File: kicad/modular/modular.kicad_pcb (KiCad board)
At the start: 2 copper layers, 50.5 x 78 mm, 53 parts, among them J1 CONN_PWR, J2 HEADER, J3 HEADER, U1 LM317, U2 LM337, U3 REF5010, U4 OPA4197

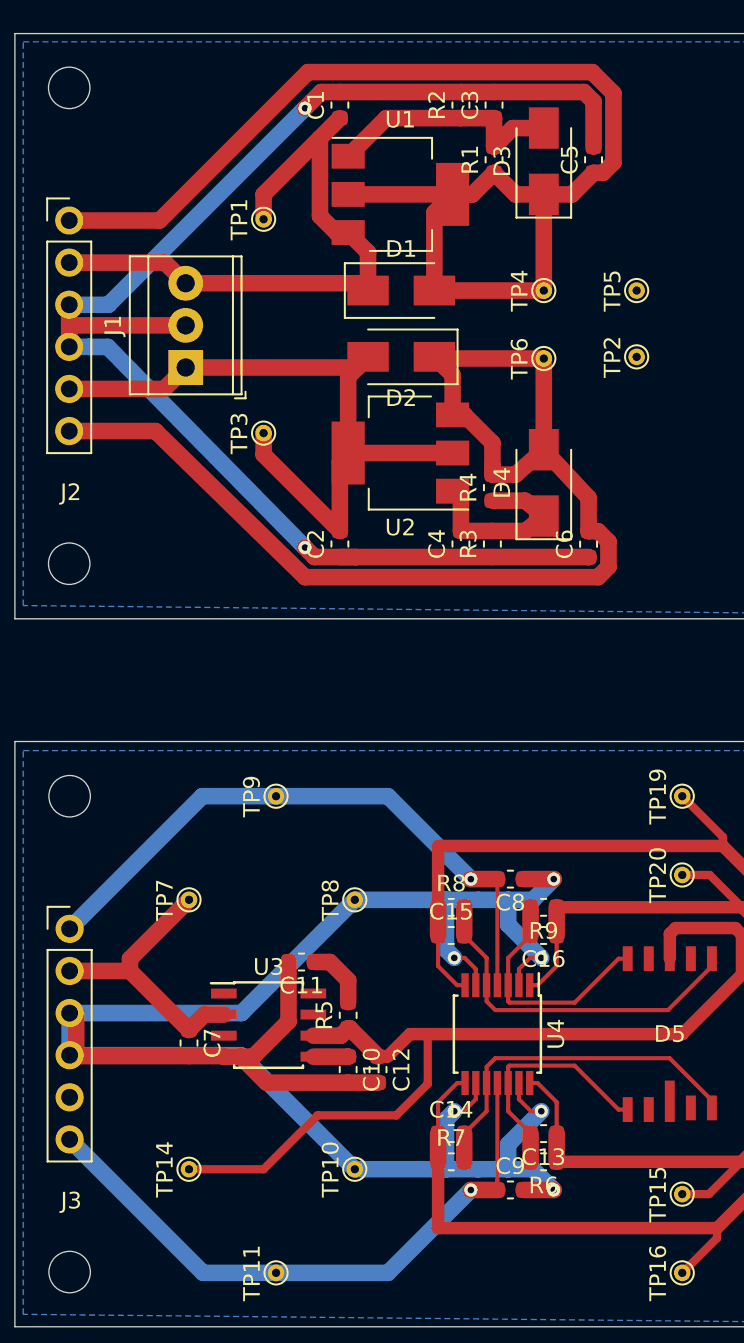
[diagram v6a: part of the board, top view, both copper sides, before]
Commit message: removed overlap of component labels in modular boards
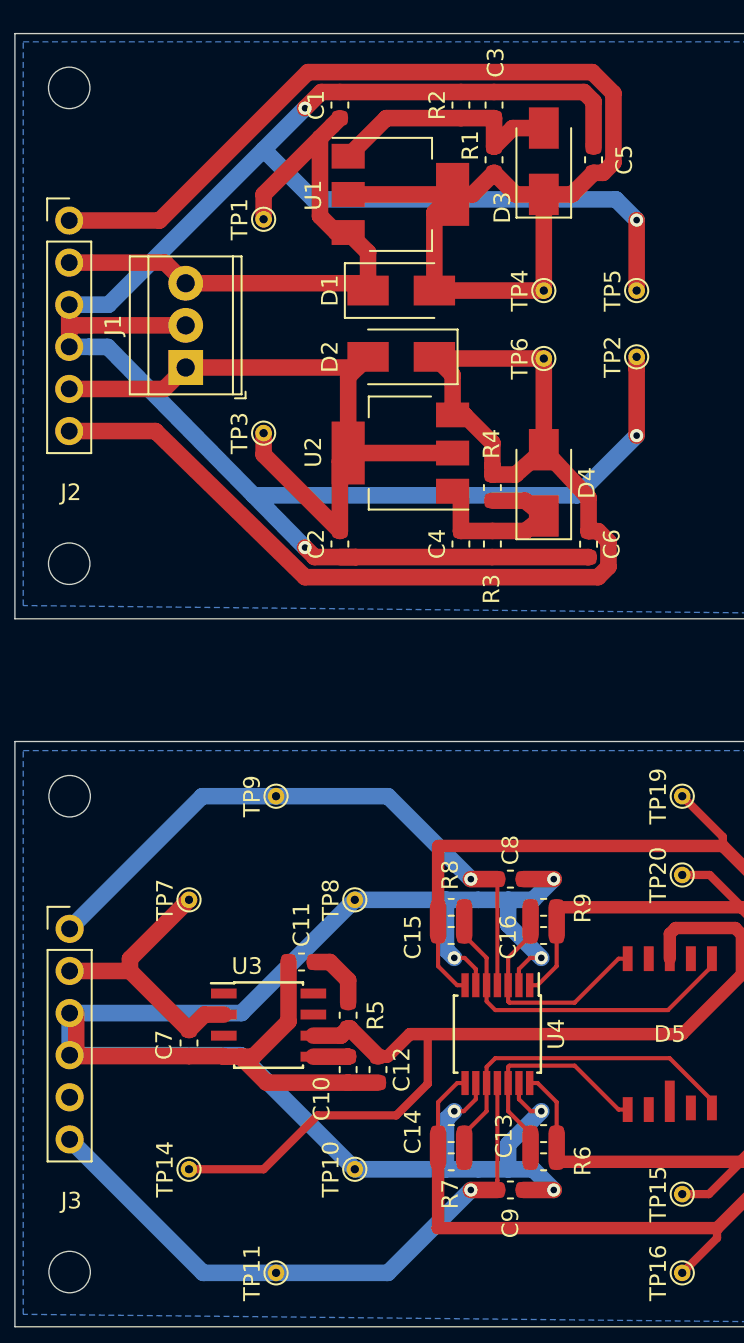
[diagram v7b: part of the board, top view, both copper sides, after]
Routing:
- net GND: track 213.7 -> 271.5 mm, vias 8 -> 10
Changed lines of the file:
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@@
     (thickness 1.6)
     (drawings 8)
-    (tracks 278)
+    (tracks 292)
     (zones 0)
     (modules 53)
@@
     (47 F.CrtYd user)
     (48 B.Fab user)
-    (49 F.Fab user)
+    (49 F.Fab user hide)
   )
   (setup
@@
     (tags "SOIC 1.27")
     (attr smd)
-    (fp_text reference U3 (at 0 -3.5) (layer F.SilkS)
+    (fp_text reference U3 (at -1.3 -3.555) (layer F.SilkS)
       (effects (font (size 1 1) (thickness 0.15)))
     )
@@
     (tags capacitor)
     (attr smd)
-    (fp_text reference C3 (at 0 -1.43 90) (layer F.SilkS)
+    (fp_text reference C3 (at 2.5625 0.1 90) (layer F.SilkS)
       (effects (font (size 1 1) (thickness 0.15)))
     )
@@
     (tags capacitor)
     (attr smd)
-    (fp_text reference C5 (at 0 -1.43 90) (layer F.SilkS)
+    (fp_text reference C5 (at 0 1.85 90) (layer F.SilkS)
       (effects (font (size 1 1) (thickness 0.15)))
     )
@@
     (tags capacitor)
     (attr smd)
-    (fp_text reference C6 (at 0 -1.43 90) (layer F.SilkS)
+    (fp_text reference C6 (at 0 1.4 90) (layer F.SilkS)
       (effects (font (size 1 1) (thickness 0.15)))
     )
@@
     (tags capacitor)
     (attr smd)
-    (fp_text reference C7 (at 0 -1.43 90) (layer F.SilkS)
+    (fp_text reference C7 (at 0.1125 1.5 270) (layer F.SilkS)
       (effects (font (size 1 1) (thickness 0.15)))
     )
@@
     (tags capacitor)
     (attr smd)
-    (fp_text reference C8 (at 0 -1.43) (layer F.SilkS)
+    (fp_text reference C8 (at 0 1.75 90) (layer F.SilkS)
       (effects (font (size 1 1) (thickness 0.15)))
     )
@@
     (tags capacitor)
     (attr smd)
-    (fp_text reference C9 (at 0 -1.43) (layer F.SilkS)
+    (fp_text reference C9 (at 0 2 90) (layer F.SilkS)
       (effects (font (size 1 1) (thickness 0.15)))
     )
@@
     (tags capacitor)
     (attr smd)
-    (fp_text reference C10 (at 0 -1.43 90) (layer F.SilkS)
+    (fp_text reference C10 (at 1.7625 1.6 90) (layer F.SilkS)
       (effects (font (size 1 1) (thickness 0.15)))
     )
@@
     (tags capacitor)
     (attr smd)
-    (fp_text reference C11 (at 0 -1.43) (layer F.SilkS)
+    (fp_text reference C11 (at 0 2.25 90) (layer F.SilkS)
       (effects (font (size 1 1) (thickness 0.15)))
     )
@@
     (tags capacitor)
     (attr smd)
-    (fp_text reference C13 (at 0 -1.43) (layer F.SilkS)
+    (fp_text reference C13 (at 2.3875 -0.15 90) (layer F.SilkS)
       (effects (font (size 1 1) (thickness 0.15)))
     )
@@
     (tags capacitor)
     (attr smd)
-    (fp_text reference C14 (at 0 -1.43) (layer F.SilkS)
+    (fp_text reference C14 (at -2.3125 -0.1 90) (layer F.SilkS)
       (effects (font (size 1 1) (thickness 0.15)))
     )
@@
     (tags capacitor)
     (attr smd)
-    (fp_text reference C15 (at 0 -1.43) (layer F.SilkS)
+    (fp_text reference C15 (at -2.3125 0.1 90) (layer F.SilkS)
       (effects (font (size 1 1) (thickness 0.15)))
     )
@@
     (tags capacitor)
     (attr smd)
-    (fp_text reference C16 (at 0 -1.43) (layer F.SilkS)
+    (fp_text reference C16 (at 2.1375 -0.1 90) (layer F.SilkS)
       (effects (font (size 1 1) (thickness 0.15)))
     )
@@
     (tags "Diode SMA (DO-214AC)")
     (attr smd)
-    (fp_text reference D1 (at 0 -2.5) (layer F.SilkS)
+    (fp_text reference D1 (at -4.3 0 90) (layer F.SilkS)
       (effects (font (size 1 1) (thickness 0.15)))
     )
@@
     (tags "Diode SMA (DO-214AC)")
     (attr smd)
-    (fp_text reference D2 (at 0 -2.5) (layer F.SilkS)
+    (fp_text reference D2 (at 4.3 0 90) (layer F.SilkS)
       (effects (font (size 1 1) (thickness 0.15)))
     )
@@
     (tags "Diode SMA (DO-214AC)")
     (attr smd)
-    (fp_text reference D3 (at 0 -2.5 90) (layer F.SilkS)
+    (fp_text reference D3 (at -2.8 -2.5 90) (layer F.SilkS)
       (effects (font (size 1 1) (thickness 0.15)))
     )
@@
     (tags "Diode SMA (DO-214AC)")
     (attr smd)
-    (fp_text reference D4 (at 0 -2.5 90) (layer F.SilkS)
+    (fp_text reference D4 (at 0 2.6 90) (layer F.SilkS)
       (effects (font (size 1 1) (thickness 0.15)))
     )
@@
     (tags resistor)
     (attr smd)
-    (fp_text reference R1 (at 0 -1.43 90) (layer F.SilkS)
+    (fp_text reference R1 (at 0.8625 -1.43 90) (layer F.SilkS)
       (effects (font (size 1 1) (thickness 0.15)))
     )
@@
     (tags resistor)
     (attr smd)
-    (fp_text reference R3 (at 0 -1.43 90) (layer F.SilkS)
+    (fp_text reference R3 (at -2.7125 -0.05 90) (layer F.SilkS)
       (effects (font (size 1 1) (thickness 0.15)))
     )
@@
     (tags resistor)
     (attr smd)
-    (fp_text reference R4 (at 0 -1.43 90) (layer F.SilkS)
+    (fp_text reference R4 (at 2.6375 -0.05 90) (layer F.SilkS)
       (effects (font (size 1 1) (thickness 0.15)))
     )
@@
     (tags resistor)
     (attr smd)
-    (fp_text reference R5 (at 0 -1.43 90) (layer F.SilkS)
+    (fp_text reference R5 (at 0 1.65 90) (layer F.SilkS)
       (effects (font (size 1 1) (thickness 0.15)))
     )
@@
     (tags resistor)
     (attr smd)
-    (fp_text reference R6 (at 0 -1.43) (layer F.SilkS)
+    (fp_text reference R6 (at -2.3625 0.05 90) (layer F.SilkS)
       (effects (font (size 1 1) (thickness 0.15)))
     )
@@
     (tags resistor)
     (attr smd)
-    (fp_text reference R7 (at 0 -1.43) (layer F.SilkS)
+    (fp_text reference R7 (at -0.0625 1.95 90) (layer F.SilkS)
       (effects (font (size 1 1) (thickness 0.15)))
     )
@@
     (tags resistor)
     (attr smd)
-    (fp_text reference R8 (at 0 -1.43) (layer F.SilkS)
+    (fp_text reference R8 (at -0.0625 -1.95 90) (layer F.SilkS)
       (effects (font (size 1 1) (thickness 0.15)))
     )
@@
     (tags resistor)
     (attr smd)
-    (fp_text reference R9 (at 0 -1.43) (layer F.SilkS)
+    (fp_text reference R9 (at -2.3625 -0.05 90) (layer F.SilkS)
       (effects (font (size 1 1) (thickness 0.15)))
     )
@@
     (tags "CMS SOT")
     (attr smd)
-    (fp_text reference U1 (at 0 -4.5) (layer F.SilkS)
+    (fp_text reference U1 (at -5.25 0.05 90) (layer F.SilkS)
       (effects (font (size 1 1) (thickness 0.15)))
     )
@@
     (tags "CMS SOT")
     (attr smd)
-    (fp_text reference U2 (at 0 -4.5) (layer F.SilkS)
+    (fp_text reference U2 (at 5.25 0.05 90) (layer F.SilkS)
       (effects (font (size 1 1) (thickness 0.15)))
     )
@@
   (segment (start 105 134.175) (end 98.255 134.175) (width 1) (layer F.Cu) (net 2))
   (segment (start 97.775001 88.855001) (end 100.144999 88.855001) (width 1) (layer B.Cu) (net 2))
-  (segment (start 100.144999 88.855001) (end 112 77) (width 1) (layer B.Cu) (net 2))
   (segment (start 112 77) (end 112 77) (width 1) (layer B.Cu) (net 2))
   (via (at 112 77) (size 0.8) (drill 0.4) (layers F.Cu B.Cu) (net 2))
@@
   (segment (start 98.977082 91.395001) (end 97.775001 91.395001) (width 1) (layer B.Cu) (net 2))
   (segment (start 112 103.5) (end 112 103.5) (width 1) (layer B.Cu) (net 2))
-  (segment (start 112 103.5) (end 100.1 91.4) (width 1) (layer B.Cu) (net 2))
   (via (at 112 103.5) (size 0.8) (drill 0.4) (layers F.Cu B.Cu) (net 2))
   (segment (start 112.575 104.075) (end 115.075 104.075) (width 1) (layer F.Cu) (net 2))
@@
   (segment (start 122.44707 141) (end 124.25 141) (width 1) (layer B.Cu) (net 2))
   (segment (start 124.25 141) (end 125.75 141) (width 1) (layer B.Cu) (net 2))
+  (segment (start 132 88) (end 132 83.75) (width 1) (layer F.Cu) (net 2))
+  (segment (start 132 83.75) (end 132 83.75) (width 1) (layer F.Cu) (net 2))
+  (via (at 132 83.75) (size 0.8) (drill 0.4) (layers F.Cu B.Cu) (net 2))
+  (segment (start 112.499999 82.499999) (end 109.5 79.5) (width 1) (layer B.Cu) (net 2))
+  (segment (start 130.749999 82.499999) (end 112.499999 82.499999) (width 1) (layer B.Cu) (net 2))
+  (segment (start 132 83.75) (end 130.749999 82.499999) (width 1) (layer B.Cu) (net 2))
+  (segment (start 109.5 79.5) (end 112 77) (width 1) (layer B.Cu) (net 2))
+  (segment (start 100.144999 88.855001) (end 109.5 79.5) (width 1) (layer B.Cu) (net 2))
+  (segment (start 132 92) (end 132 92.707106) (width 1) (layer F.Cu) (net 2))
+  (segment (start 132 92.707106) (end 132 96.75) (width 1) (layer F.Cu) (net 2))
+  (segment (start 132 96.75) (end 132 96.75) (width 1) (layer F.Cu) (net 2))
+  (via (at 132 96.75) (size 0.8) (drill 0.4) (layers F.Cu B.Cu) (net 2))
+  (segment (start 112 103.5) (end 108.901042 100.348958) (width 1) (layer B.Cu) (net 2))
+  (segment (start 128.401042 100.348958) (end 132 96.75) (width 1) (layer B.Cu) (net 2))
+  (segment (start 108.901042 100.348958) (end 128.401042 100.348958) (width 1) (layer B.Cu) (net 2))
+  (segment (start 108.901042 100.348958) (end 100.1 91.4) (width 1) (layer B.Cu) (net 2))
   (segment (start 109.5 97.9) (end 114.1 102.5) (width 1) (layer F.Cu) (net 3))
   (segment (start 109.5 96.6) (end 109.5 97.9) (width 1) (layer F.Cu) (net 3))
@@
     (connect_pads (clearance 0.508))
     (min_thickness 0.254)
-    (fill yes (arc_segments 32) (thermal_gap 0.508) (thermal_bridge_width 0.508))
+    (fill (arc_segments 32) (thermal_gap 0.508) (thermal_bridge_width 0.508))
     (polygon
       (pts
@@
     (connect_pads (clearance 0.508))
     (min_thickness 0.254)
-    (fill yes (arc_segments 32) (thermal_gap 0.508) (thermal_bridge_width 0.508))
+    (fill (arc_segments 32) (thermal_gap 0.508) (thermal_bridge_width 0.508))
     (polygon
       (pts

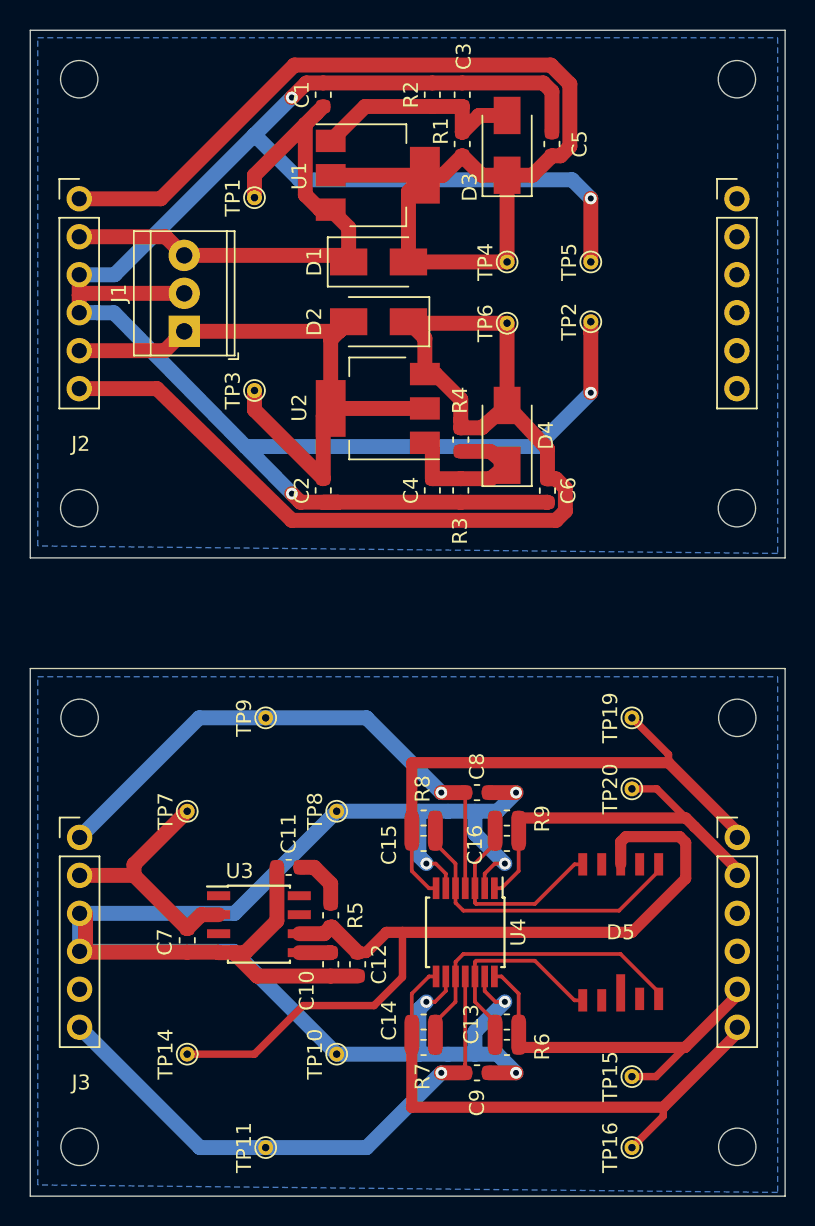
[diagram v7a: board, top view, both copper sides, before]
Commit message: fixed opamp input terminal connection, connected some caps directly to gnd through vias
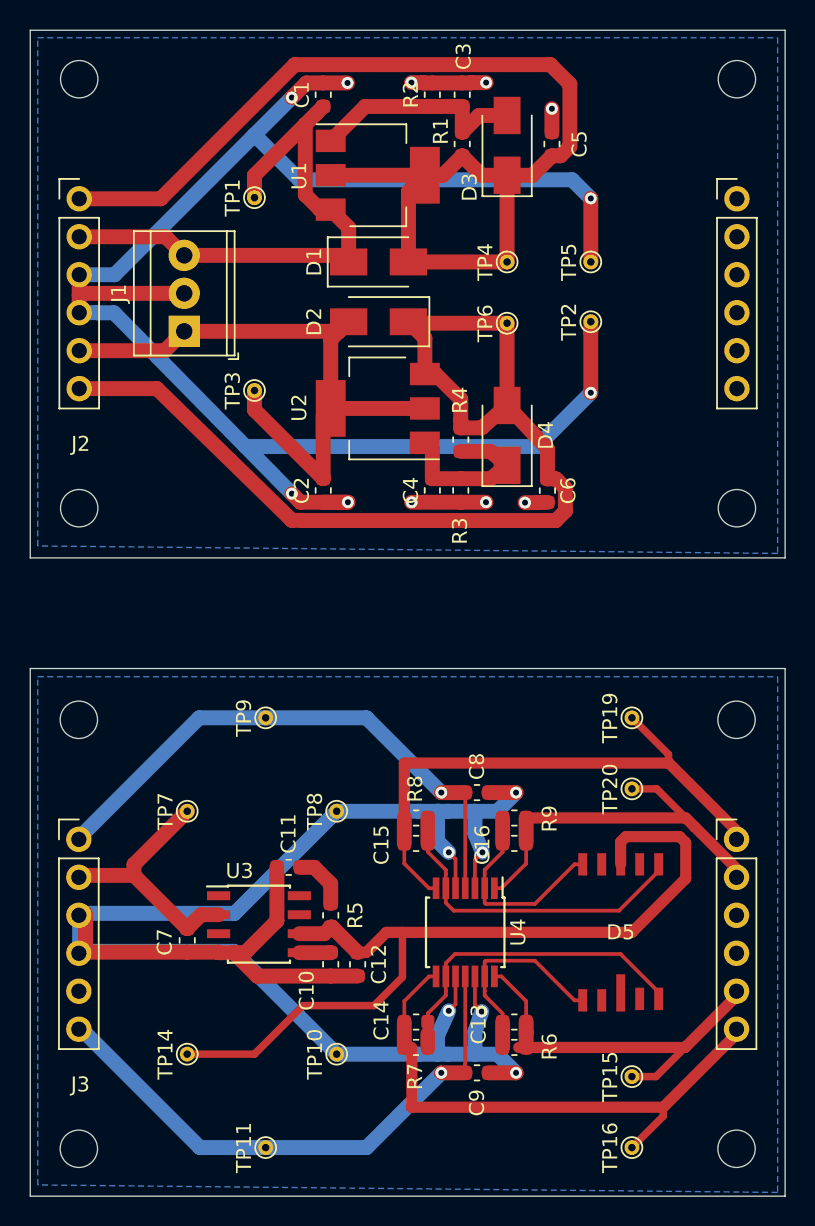
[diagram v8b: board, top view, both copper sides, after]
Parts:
- moved C13 0.50 mm to (126.9, 138.8)
- moved C14 0.50 mm to (120.3, 138.8)
- moved C15 0.50 mm to (120.3, 126.9)
- moved C16 0.50 mm to (126.9, 126.9)
- moved R6 0.50 mm to (126.9, 140.6)
- moved R7 0.50 mm to (120.3, 140.6)
- moved R8 0.50 mm to (120.3, 125.2)
- moved R9 0.50 mm to (126.9, 125.2)
- moved J3 0.14 mm to (97.8, 126.6)
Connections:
- U4 pad 10: Net-(C14-Pad2) -> GND
- U4 pad 12: Net-(C13-Pad2) -> GND
- U4 pad 13: GND -> Net-(C13-Pad2)
- U4 pad 2: GND -> Net-(C16-Pad2)
- U4 pad 3: Net-(C16-Pad2) -> GND
- U4 pad 5: Net-(C15-Pad2) -> GND
- U4 pad 6: GND -> Net-(C15-Pad2)
- U4 pad 9: GND -> Net-(C14-Pad2)
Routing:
- net GND: track 271.5 -> 251.0 mm, vias 10 -> 18
- net /Detector/X1: track 26.7 -> 27.7 mm
- net Net-(C16-Pad2): track 14.6 -> 13.9 mm
- net Net-(C13-Pad2): track 14.6 -> 13.9 mm
- net /Detector/X2: track 37.6 -> 38.3 mm
- net Net-(C15-Pad2): track 21.6 -> 22.2 mm
- net Net-(C14-Pad2): track 21.6 -> 22.1 mm
